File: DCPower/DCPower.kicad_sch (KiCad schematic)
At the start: 105 parts, among them IC1 LTC4417CUF#PBF, J1 USB_C_Receptacle_USB2.0_14P, J2 XT30, J4 Barrel_Jack_Switch, Q1 DMP4025LSD-13, Q2 DMP4025LSD-13, Q3 DMP4025LSD-13, Q4 DMP4025LSD-13, Q5 DMP4025LSD-13, Q6 2N7002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

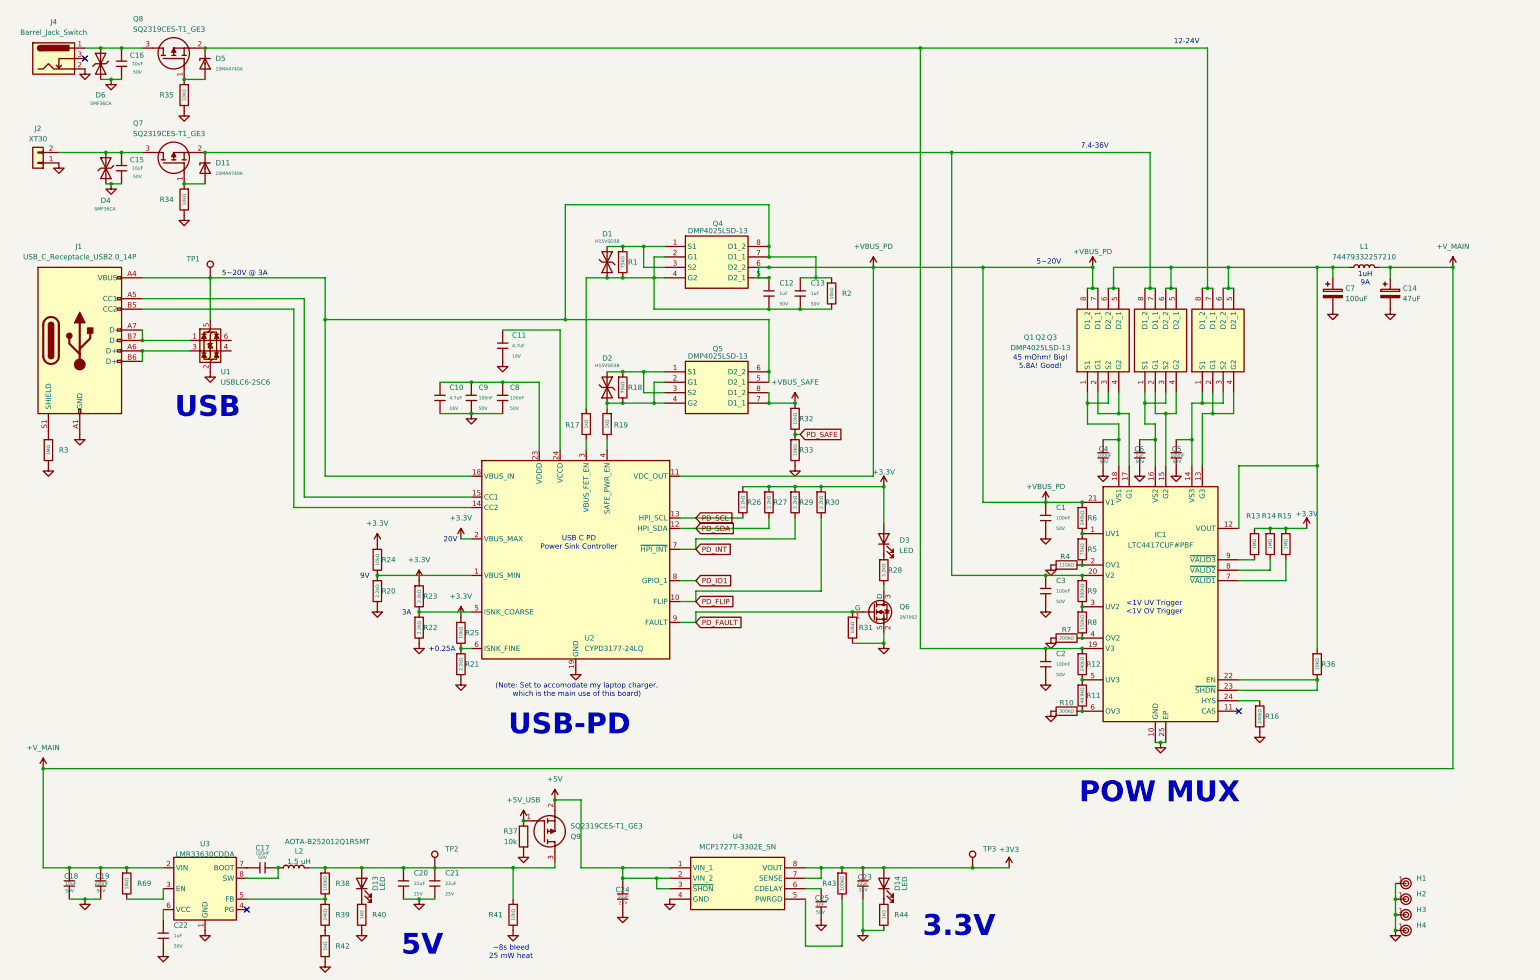
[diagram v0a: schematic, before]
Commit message: More Power Path, fixed filter
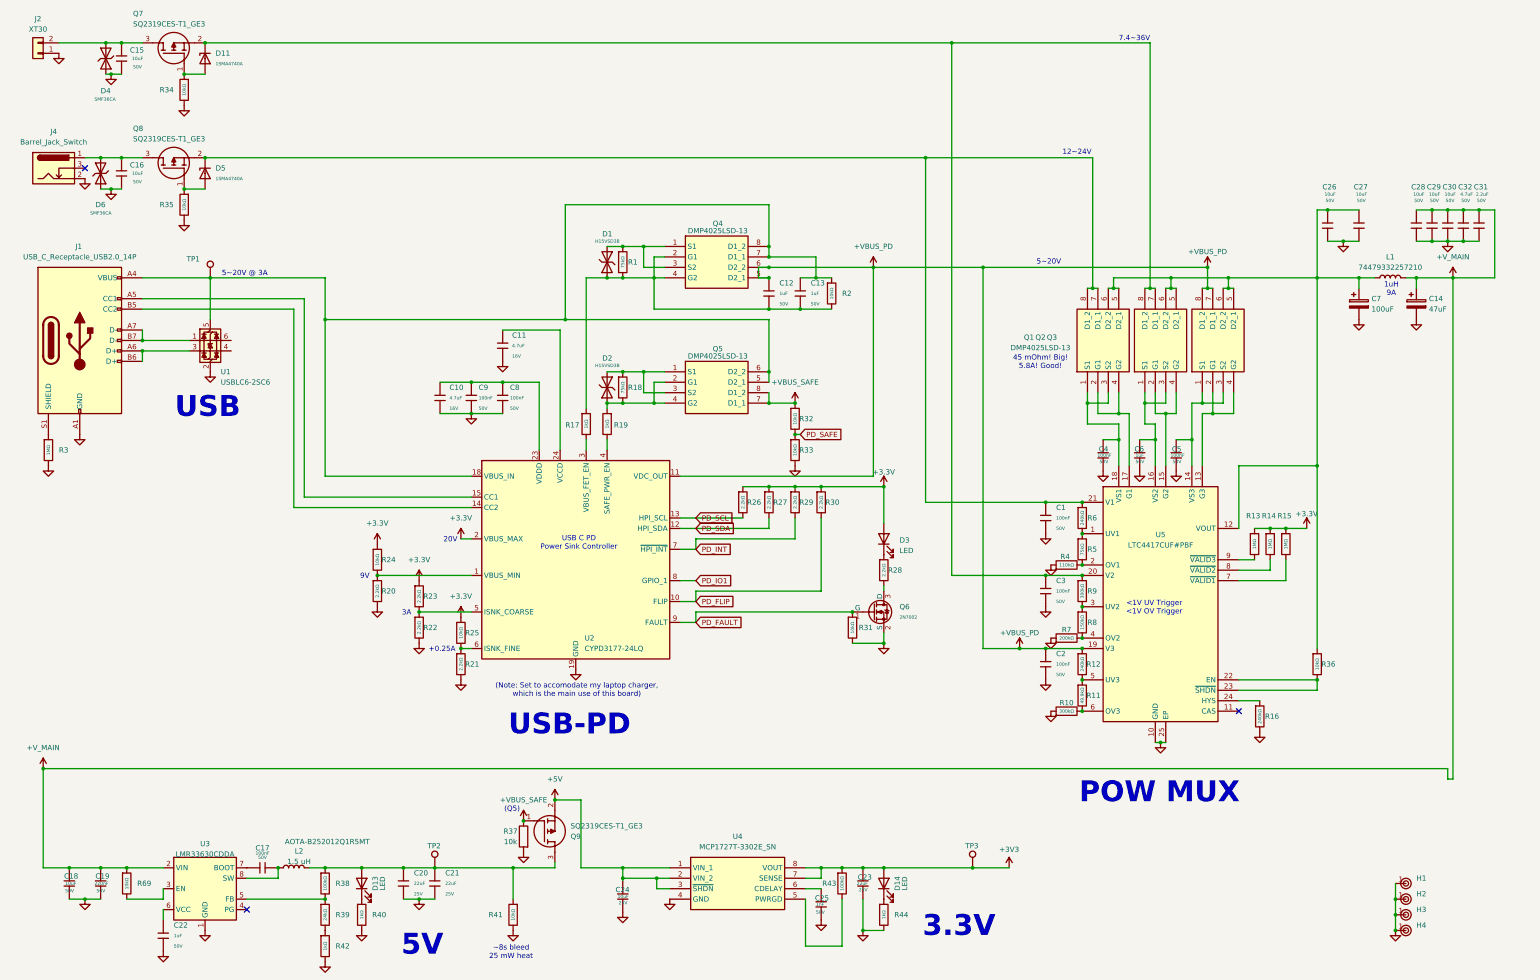
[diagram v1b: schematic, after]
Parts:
- added C26, C27, C28, C29, C30: 10uF, PCM_JLCPCB:C_1206, symbol PCM_JLCPCB-Capacitors:1206,10uF
- added C31: 2.2uF, PCM_JLCPCB:C_0805, symbol PCM_JLCPCB-Capacitors:0805,2.2uF
- added C32: 4.7uF, PCM_JLCPCB:C_1206, symbol PCM_JLCPCB-Capacitors:1206,4.7uF
- renumbered IC1 to U5
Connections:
- net +5V_USB is gone; now on net +VBUS_SAFE: Q9.1 (G), R37.1
- net +VBUS_PD: now also C2.1, Q3.7 (D1_1), Q3.8 (D1_2), R12.1, U5.19 (V3); no longer C1.1, Q1.7 (D1_1), Q1.8 (D1_2), R6.1, U5.21 (V1)
- net +V_MAIN: now also C28.1, C29.1, C30.1, C31.1, C32.1
- net GND: now also C26.2, C27.2, C28.2, C29.2, C30.2, C31.2, C32.2
- net at C7.1, L1.1, Q1.5 (D2_1)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: now also C26.1, C27.1
- new net: C1.1, D5.1, Q1.7 (D1_1), Q1.8 (D1_2), Q8.2 (S), R6.1, U5.21 (V1)
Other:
- note added: "(Q5)"
- note added: "12~24V"
- note added: "7.4~36V"
- note removed: "12-24V"
- note removed: "7.4-36V"
- moved on the sheet: C14, C15, C16, C7, D11, D4, D5, D6, J2, J4, L1, Q7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

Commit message: 2nd Order RLC Simulation
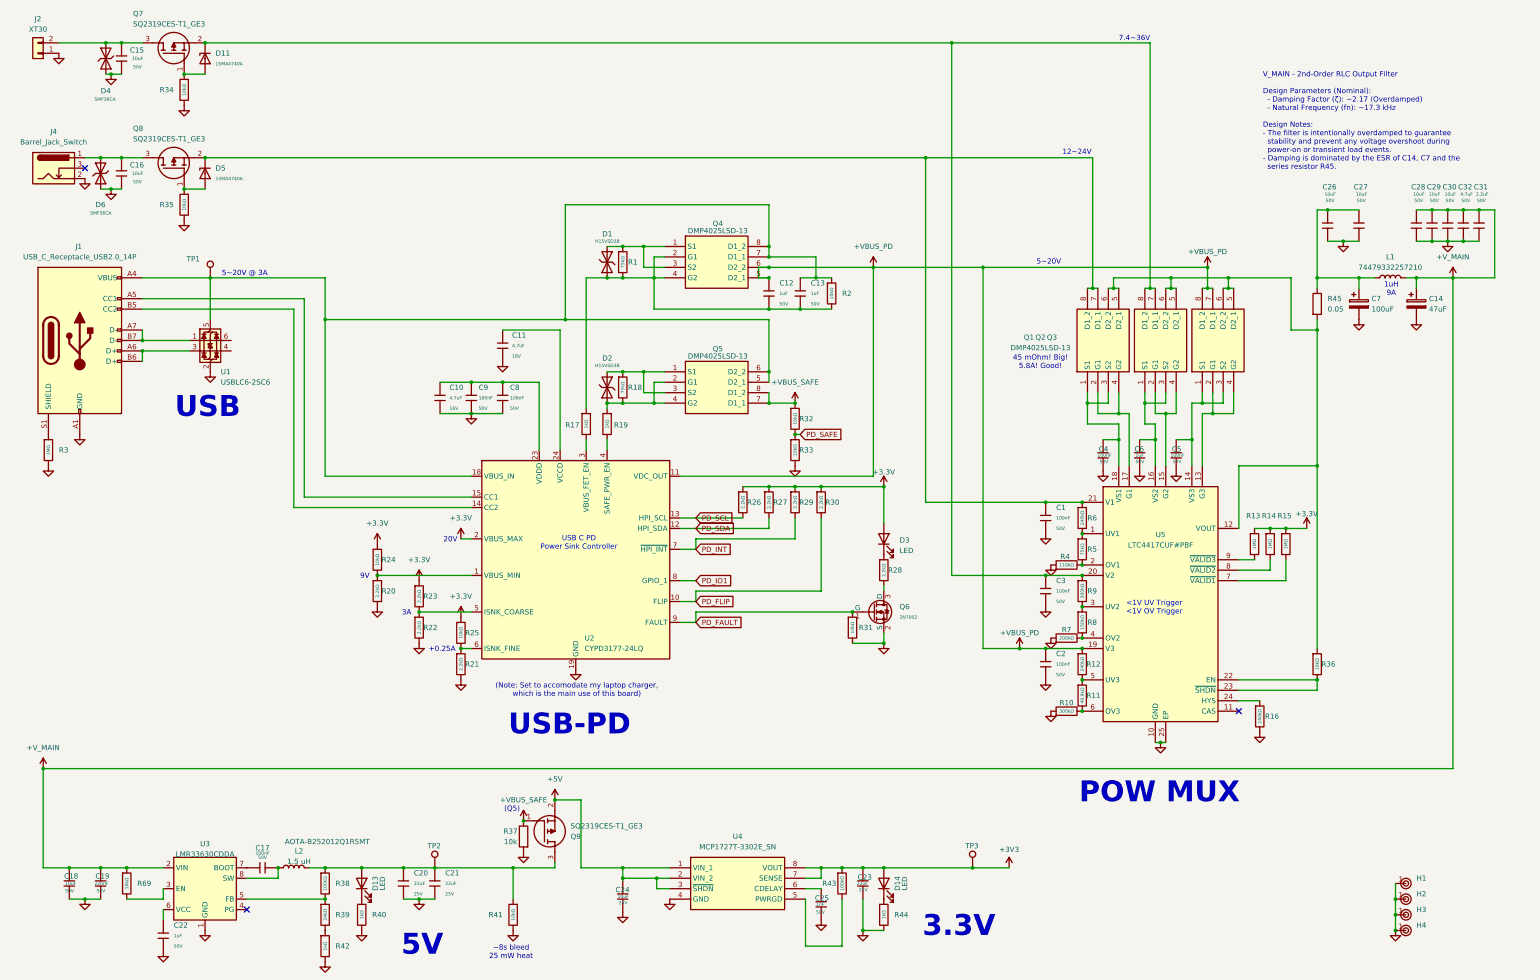
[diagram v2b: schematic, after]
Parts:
- added R45: 0.05, symbol Device:R
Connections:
- net at Q1.5 (D2_1), Q1.6 (D2_2), Q2.5 (D2_1)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: now also R45.2; no longer C26.1, C27.1, C7.1, L1.1
- new net: C26.1, C27.1, C7.1, L1.1, R45.1
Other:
- note added: "V_MAIN - 2nd-Order RLC Output Filter Design Parameters (Nominal): - Damping Factor (ζ): ~2.17 (Overdamped) - Natural Frequency (fn): ~17.3 kHz Design Notes: - The filter is intentionally overdamped to guarantee stability and prevent any voltage overshoot during power-on or transient load events. - Damping is dominated by the ESR of C14, C7 and the series resistor R45."
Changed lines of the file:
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@@
 		)
 	)
+	(text "V_MAIN - 2nd-Order RLC Output Filter\n\nDesign Parameters (Nominal):\n  - Damping Factor (ζ): ~2.17 (Overdamped)\n  - Natural Frequency (fn): ~17.3 kHz\n\nDesign Notes:\n- The filter is intentionally overdamped to guarantee\n  stability and prevent any voltage overshoot during\n  power-on or transient load events.\n- Damping is dominated by the ESR of C14, C7 and the\n  series resistor R45."
+		(exclude_from_sim no)
+		(at 350.012 41.91 0)
+		(effects
+			(font
+				(size 1.27 1.27)
+			)
+			(justify left)
+		)
+	)
 	(text "20V"
 		(exclude_from_sim no)
@@
 	)
 	(junction
+		(at 363.22 92.71)
+		(diameter 0)
+		(color 0 0 0 0)
+	)
+	(junction
 		(at 323.85 119.38)
 		(diameter 0)
@@
 	)
 	(junction
-		(at 341.63 80.01)
-		(diameter 0)
-		(color 0 0 0 0)
-	)
-	(junction
 		(at 121.92 223.52)
 		(diameter 0)
@@
 	)
 	(junction
+		(at 341.63 80.01)
+		(diameter 0)
+		(color 0 0 0 0)
+	)
+	(junction
 		(at 190.5 110.49)
 		(diameter 0)
@@
 	(wire
 		(pts
-			(xy 394.97 199.39) (xy 53.34 199.39)
+			(xy 53.34 199.39) (xy 396.24 199.39)
 		)
 		(stroke
@@
 	(wire
 		(pts
+			(xy 363.22 92.71) (xy 363.22 90.17)
+		)
+		(stroke
+			(width 0)
+			(type default)
+		)
+	)
+	(wire
+		(pts
 			(xy 121.92 223.52) (xy 130.81 223.52)
 		)
@@
 	(wire
 		(pts
+			(xy 363.22 92.71) (xy 363.22 125.73)
+		)
+		(stroke
+			(width 0)
+			(type default)
+		)
+	)
+	(wire
+		(pts
 			(xy 257.81 166.37) (xy 257.81 168.91)
 		)
@@
 	(wire
 		(pts
-			(xy 363.22 80.01) (xy 363.22 125.73)
+			(xy 363.22 80.01) (xy 363.22 82.55)
 		)
 		(stroke
@@
 	(wire
 		(pts
-			(xy 396.24 80.01) (xy 396.24 201.93)
+			(xy 396.24 80.01) (xy 396.24 199.39)
 		)
 		(stroke
@@
 	(wire
 		(pts
+			(xy 356.87 92.71) (xy 356.87 80.01)
+		)
+		(stroke
+			(width 0)
+			(type default)
+		)
+	)
+	(wire
+		(pts
 			(xy 236.22 110.49) (xy 229.87 110.49)
 		)
@@
 	(wire
 		(pts
-			(xy 341.63 80.01) (xy 363.22 80.01)
-		)
-		(stroke
-			(width 0)
-			(type default)
-		)
-	)
-	(wire
-		(pts
 			(xy 391.16 71.12) (xy 394.97 71.12)
 		)
@@
 	(wire
 		(pts
+			(xy 363.22 92.71) (xy 356.87 92.71)
+		)
+		(stroke
+			(width 0)
+			(type default)
+		)
+	)
+	(wire
+		(pts
 			(xy 323.85 115.57) (xy 323.85 119.38)
 		)
@@
 	(wire
 		(pts
-			(xy 394.97 201.93) (xy 394.97 199.39)
-		)
-		(stroke
-			(width 0)
-			(type default)
-		)
-	)
-	(wire
-		(pts
 			(xy 92.71 22.86) (xy 274.32 22.86)
 		)
@@
 	(wire
 		(pts
-			(xy 394.97 201.93) (xy 396.24 201.93)
-		)
-		(stroke
-			(width 0)
-			(type default)
-		)
-	)
-	(wire
-		(pts
 			(xy 355.6 153.67) (xy 355.6 148.59)
 		)
@@
 	(wire
 		(pts
+			(xy 356.87 80.01) (xy 341.63 80.01)
+		)
+		(stroke
+			(width 0)
+			(type default)
+		)
+	)
+	(wire
+		(pts
 			(xy 201.93 87.63) (xy 201.93 80.01)
 		)
@@
 					(unit 1)
 				)
+			)
+		)
+	)
+	(symbol
+		(lib_id "Device:R")
+		(at 363.22 86.36 0)
+		(unit 1)
+		(exclude_from_sim no)
+		(in_bom yes)
+		(on_board yes)
+		(dnp no)
+		(fields_autoplaced yes)
+		(property "Reference" "R45"
+			(at 365.76 85.0899 0)
+			(effects
+				(font
+					(size 1.27 1.27)
+				)
+				(justify left)
+			)
+		)
+		(property "Value" "0.05"
+			(at 365.76 87.6299 0)
+			(effects
+				(font
+					(size 1.27 1.27)
+				)
+				(justify left)
+			)
+		)
+		(property "Footprint" ""
+			(at 361.442 86.36 90)
+			(effects
+				(font
+					(size 1.27 1.27)
+				)
+				(hide yes)
+			)
+		)
+		(property "Datasheet" "~"
+			(at 363.22 86.36 0)
+			(effects
+				(font
+					(size 1.27 1.27)
+				)
+				(hide yes)
+			)
+		)
+		(property "Description" "Resistor"
+			(at 363.22 86.36 0)
+			(effects
+				(font
+					(size 1.27 1.27)
+				)
+				(hide yes)
+			)
+		)
+		(pin "1"
+		)
+		(pin "2"
+		)
+		(instances
+			(project ""
+				(path "/eca3382c-8ef0-49cd-b01d-b9c14b82da03"
+					(reference "R45")
+					(unit 1)
+				)

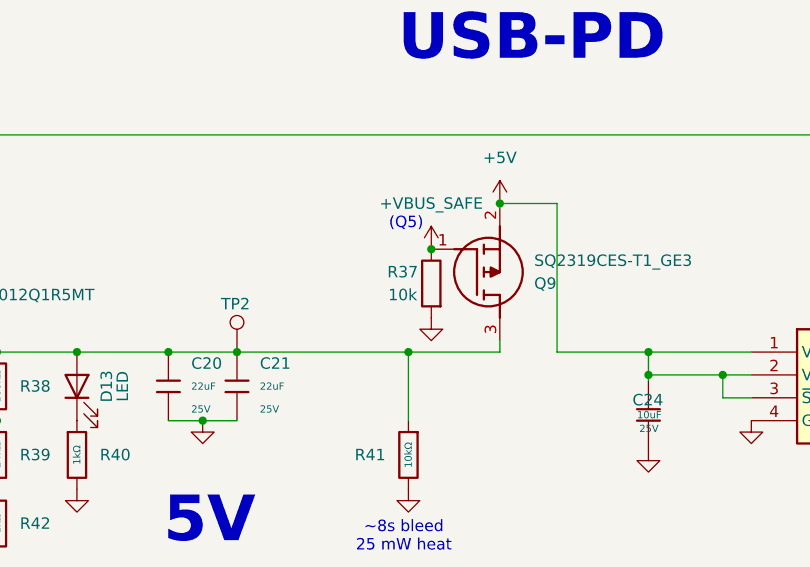
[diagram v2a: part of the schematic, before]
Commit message: Forked into Simple 1 input version
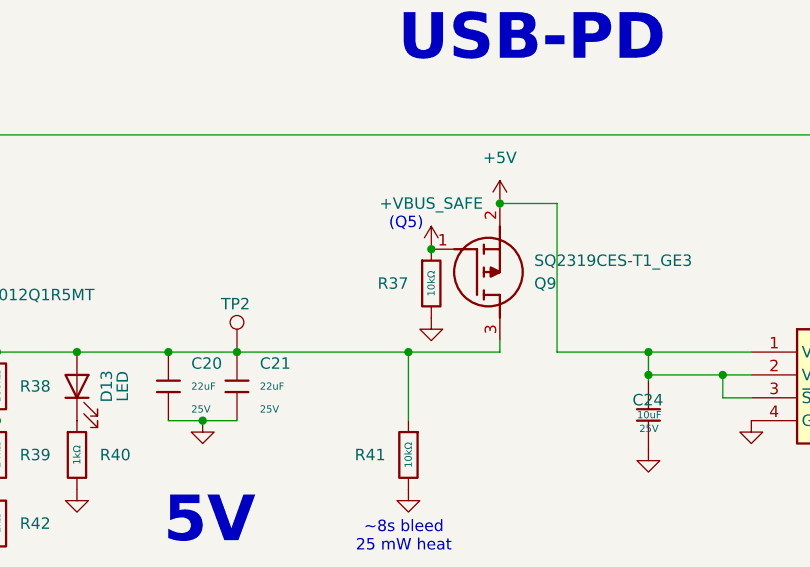
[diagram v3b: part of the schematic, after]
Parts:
- removed R37: 10k, Resistor_SMD:R_0402_1005Metric, symbol Device:R
- added R37: 10kΩ, PCM_JLCPCB:R_0603, symbol PCM_JLCPCB-Resistors:0603,10kΩ
- Q9: footprint Temp-Monitor:SOT95P237X112-3N -> SwiftModules:SOT95P237X112-3N
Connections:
- net +VBUS_SAFE: now also R37.1
- net GND: now also R37.2
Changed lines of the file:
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@@
 	)
 	(junction
+		(at 170.18 212.09)
+		(diameter 0)
+		(color 0 0 0 0)
+	)
+	(junction
 		(at 267.97 50.8)
 		(diameter 0)
@@
 	)
 	(junction
-		(at 170.18 212.09)
-		(diameter 0)
-		(color 0 0 0 0)
-	)
-	(junction
 		(at 391.16 63.5)
 		(diameter 0)
@@
 			)
 		)
-		(property "Footprint" "Temp-Monitor:SOT95P237X112-3N"
+		(property "Footprint" "SwiftModules:SOT95P237X112-3N"
 			(at 181.61 113.36 0)
 			(effects
@@
 	)
 	(symbol
-		(lib_id "Device:R")
-		(at 170.18 215.9 0)
-		(mirror y)
-		(unit 1)
-		(exclude_from_sim no)
-		(in_bom yes)
-		(on_board yes)
-		(dnp no)
-		(property "Reference" "R37"
-			(at 167.005 214.63 0)
-			(effects
-				(font
-					(size 1.27 1.27)
-				)
-			)
-		)
-		(property "Value" "10k"
-			(at 167.005 217.17 0)
-			(effects
-				(font
-					(size 1.27 1.27)
-				)
-			)
-		)
-		(property "Footprint" "Resistor_SMD:R_0402_1005Metric"
-			(at 171.958 215.9 90)
-			(effects
-				(font
-					(size 1.27 1.27)
-				)
-				(hide yes)
-			)
-		)
-		(property "Datasheet" "~"
-			(at 170.18 215.9 0)
-			(effects
-				(font
-					(size 1.27 1.27)
-				)
-				(hide yes)
-			)
-		)
-		(property "Description" "Resistor"
-			(at 170.18 215.9 0)
-			(effects
-				(font
-					(size 1.27 1.27)
-				)
-				(hide yes)
-			)
-		)
-		(pin "2"
-		)
-		(pin "1"
-		)
-		(instances
-			(project "DCPower"
-				(path "/eca3382c-8ef0-49cd-b01d-b9c14b82da03"
-					(reference "R37")
-					(unit 1)
-				)
-			)
-		)
-	)
-	(symbol
 		(lib_id "PCM_JLCPCB-Capacitors:0603,100nF")
 		(at 157.48 109.22 0)
@@
 					(unit 1)
 				)
+			)
+		)
+	)
+	(symbol
+		(lib_name "0603,10kΩ_1")
+		(lib_id "PCM_JLCPCB-Resistors:0603,10kΩ")
+		(at 170.18 215.9 0)
+		(unit 1)
+		(exclude_from_sim no)
+		(in_bom yes)
+		(on_board yes)
+		(dnp no)
+		(property "Reference" "R37"
+			(at 167.64 215.8999 0)
+			(effects
+				(font
+					(size 1.27 1.27)
+				)
+				(justify right)
+			)
+		)
+		(property "Value" "10kΩ"
+			(at 170.18 215.9 90)
+			(do_not_autoplace yes)
+			(effects
+				(font
+					(size 0.8 0.8)
+				)
+			)
+		)
+		(property "Footprint" "PCM_JLCPCB:R_0603"
+			(at 168.402 215.9 90)
+			(effects
+				(font
+					(size 1.27 1.27)
+				)
+				(hide yes)
+			)
+		)
+		(property "Datasheet" "https://www.lcsc.com/datasheet/lcsc_datasheet_2206010045_UNI-ROYAL-Uniroyal-Elec-0603WAF1002T5E_C25804.pdf"
+			(at 170.18 215.9 0)
+			(effects
+				(font
+					(size 1.27 1.27)
+				)
+				(hide yes)
+			)
+		)
+		(property "Description" "100mW Thick Film Resistors 75V ±100ppm/°C ±1% 10kΩ 0603 Chip Resistor - Surface Mount ROHS"
+			(at 170.18 215.9 0)
+			(effects
+				(font
+					(size 1.27 1.27)
+				)
+				(hide yes)
+			)
+		)
+		(property "LCSC" "C25804"
+			(at 170.18 215.9 0)
+			(effects
+				(font
+					(size 1.27 1.27)
+				)
+				(hide yes)
+			)
+		)
+		(property "Stock" "26472080"
+			(at 170.18 215.9 0)
+			(effects
+				(font
+					(size 1.27 1.27)
+				)
+				(hide yes)
+			)
+		)
+		(property "Price" "0.004USD"
+			(at 170.18 215.9 0)
+			(effects
+				(font
+					(size 1.27 1.27)
+				)
+				(hide yes)
+			)
+		)
+		(property "Process" "SMT"
+			(at 170.18 215.9 0)
+			(effects
+				(font
+					(size 1.27 1.27)
+				)
+				(hide yes)
+			)
+		)
+		(property "Minimum Qty" "20"
+			(at 170.18 215.9 0)
+			(effects
+				(font
+					(size 1.27 1.27)
+				)
+				(hide yes)
+			)
+		)
+		(property "Attrition Qty" "10"
+			(at 170.18 215.9 0)
+			(effects
+				(font
+					(size 1.27 1.27)
+				)
+				(hide yes)
+			)
+		)
+		(property "Class" "Basic Component"
+			(at 170.18 215.9 0)
+			(effects
+				(font
+					(size 1.27 1.27)
+				)
+				(hide yes)
+			)
+		)
+		(property "Category" "Resistors,Chip Resistor - Surface Mount"
+			(at 170.18 215.9 0)
+			(effects
+				(font
+					(size 1.27 1.27)
+				)
+				(hide yes)
+			)
+		)
+		(property "Manufacturer" "UNI-ROYAL(Uniroyal Elec)"
+			(at 170.18 215.9 0)
+			(effects
+				(font
+					(size 1.27 1.27)
+				)
+				(hide yes)
+			)
+		)
+		(property "Part" "0603WAF1002T5E"
+			(at 170.18 215.9 0)
+			(effects
+				(font
+					(size 1.27 1.27)
+				)
+				(hide yes)
+			)
+		)
+		(property "Resistance" "10kΩ"
+			(at 170.18 215.9 0)
+			(effects
+				(font
+					(size 1.27 1.27)
+				)
+				(hide yes)
+			)
+		)
+		(property "Power(Watts)" "100mW"
+			(at 170.18 215.9 0)
+			(effects
+				(font
+					(size 1.27 1.27)
+				)
+				(hide yes)
+			)
+		)
+		(property "Type" "Thick Film Resistors"
+			(at 170.18 215.9 0)
+			(effects
+				(font
+					(size 1.27 1.27)
+				)
+				(hide yes)
+			)
+		)
+		(property "Overload Voltage (Max)" "75V"
+			(at 170.18 215.9 0)
+			(effects
+				(font
+					(size 1.27 1.27)
+				)
+				(hide yes)
+			)
+		)
+		(property "Operating Temperature Range" "-55°C~+155°C"
+			(at 170.18 215.9 0)
+			(effects
+				(font
+					(size 1.27 1.27)
+				)
+				(hide yes)
+			)
+		)
+		(property "Tolerance" "±1%"
+			(at 170.18 215.9 0)
+			(effects
+				(font
+					(size 1.27 1.27)
+				)
+				(hide yes)
+			)
+		)
+		(property "Temperature Coefficient" "±100ppm/°C"
+			(at 170.18 215.9 0)
+			(effects
+				(font
+					(size 1.27 1.27)
+				)
+				(hide yes)
+			)
+		)
+		(pin "2"
+		)
+		(pin "1"
+		)
+		(instances
+			(project ""
+				(path "/eca3382c-8ef0-49cd-b01d-b9c14b82da03"
+					(reference "R37")
+					(unit 1)
+				)
